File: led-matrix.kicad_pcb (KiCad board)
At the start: 2 copper layers, 91 parts, among them J1 Conn_01x01_Pin, J10 Conn_01x01_Pin, J11 Conn_01x01_Pin, J12 Conn_01x01_Pin, J13 Conn_01x01_Pin, J14 Conn_01x01_Pin, J15 Conn_01x01_Pin, J16 Conn_01x01_Pin, J17 Conn_01x01_Pin, J18 Conn_01x01_Pin, J19 Conn_01x01_Pin, J2 Conn_01x01_Pin, J20 Conn_01x01_Pin, J21 Conn_01x01_Pin, J22 Conn_01x01_Pin, J23 Conn_01x01_Pin, J3 Conn_01x01_Pin, J4 Conn_01x01_Pin, J5 Conn_01x01_Pin, J6 Conn_01x01_Pin, J7 Conn_01x01_Pin, J8 Conn_01x01_Pin, J9 Conn_01x01_Pin, U1 MAX7219, U2 Pico

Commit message: feat: layout basic pcb design
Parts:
- moved J6 77.9 mm to (126.0, 65.0)
- moved J1 77.8 mm to (96.0, 65.0)
- moved J5 76.4 mm to (120.0, 65.0)
- moved J2 76.4 mm to (102.0, 65.0)
- moved J4 75.7 mm to (114.0, 65.0)
- moved J3 75.7 mm to (108.0, 65.0)
- moved J12 72.5 mm to (159.5, 64.5)
- moved J11 68.3 mm to (154.0, 64.5)
- moved J10 64.7 mm to (148.5, 64.5)
- moved J9 61.8 mm to (143.0, 64.5)
- moved J8 59.4 mm to (137.5, 64.5)
- moved J7 57.9 mm to (132.0, 64.5)
- moved J14 54.8 mm to (170.5, 64.5)
- moved J15 53.1 mm to (173.0, 71.0)
- moved J16 52.0 mm to (173.0, 76.5)
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
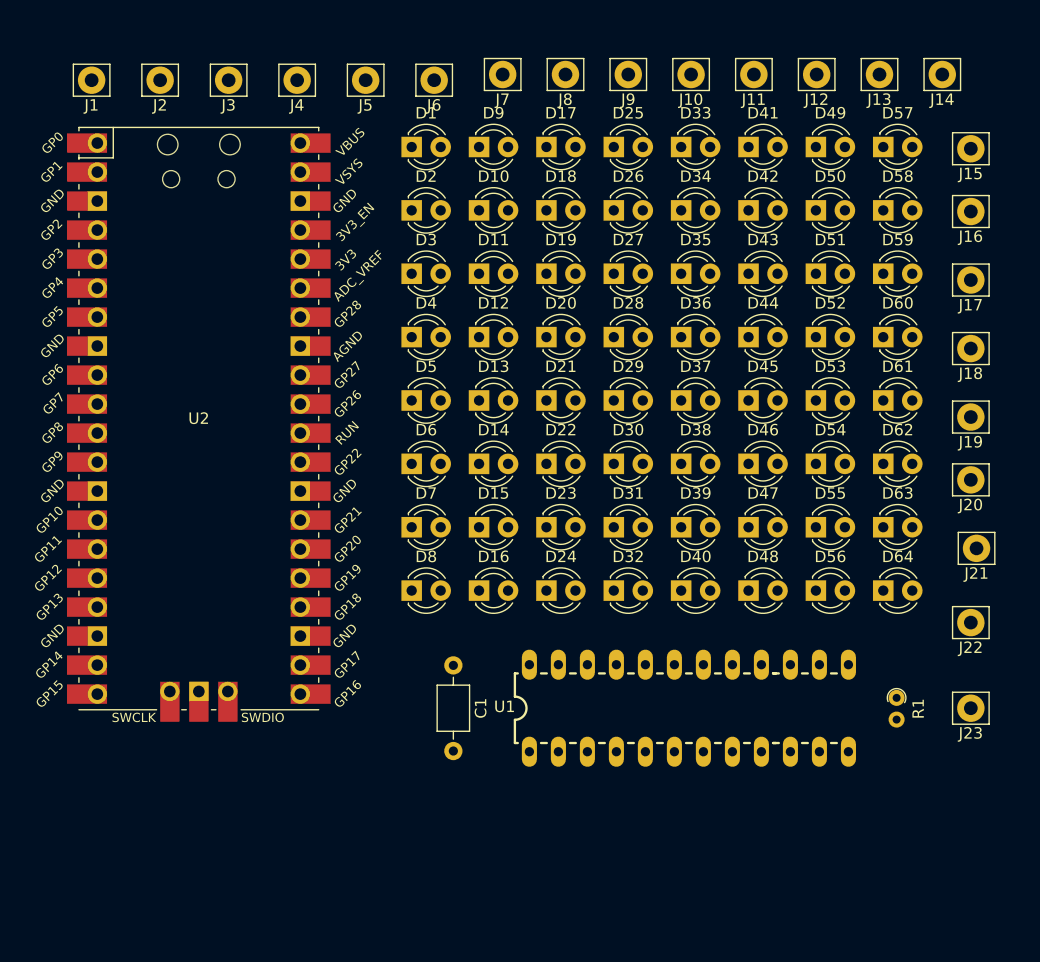
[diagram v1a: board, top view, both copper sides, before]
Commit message: chore: align and center the gpio
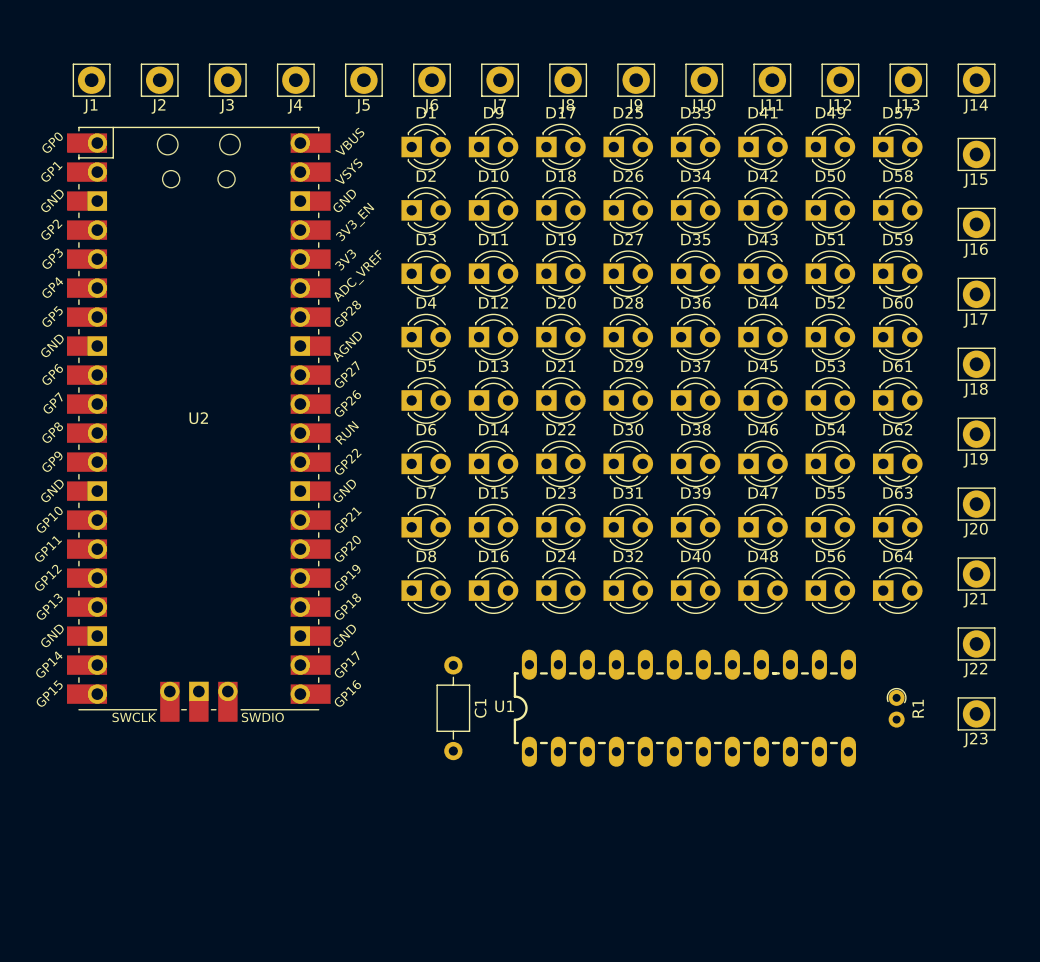
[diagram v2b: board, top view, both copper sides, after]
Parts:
- moved J14 3.04 mm to (173.5, 65.0)
- moved J13 2.59 mm to (167.5, 65.0)
- moved J21 2.25 mm to (173.5, 108.2)
- moved J20 2.18 mm to (173.5, 102.1)
- moved J12 2.14 mm to (161.6, 65.0)
- moved J22 1.94 mm to (173.5, 114.4)
- moved J11 1.69 mm to (155.6, 65.0)
- moved J19 1.58 mm to (173.5, 96.0)
- moved J18 1.46 mm to (173.5, 89.9)
- moved J17 1.35 mm to (173.5, 83.8)
- moved J10 1.26 mm to (149.7, 65.0)
- moved J16 1.23 mm to (173.5, 77.6)
- moved J9 0.85 mm to (143.7, 65.0)
- moved J15 0.71 mm to (173.5, 71.5)
- moved J23 0.71 mm to (173.5, 120.5)
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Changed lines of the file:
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@@
 	(footprint "Connector_Pin:Pin_D1.2mm_L11.3mm_W3.0mm_Flat"
 		(layer "F.Cu")
-		(at 173 100)
+		(at 173.5 102.125)
 		(descr "solder Pin_ with flat with hole, hole diameter 1.2mm, length 11.3mm, width 3.0mm")
 		(tags "solder Pin_ with flat fork")
@@
 	(footprint "Connector_Pin:Pin_D1.2mm_L11.3mm_W3.0mm_Flat"
 		(layer "F.Cu")
-		(at 137.5 64.5)
+		(at 137.730766 65)
 		(descr "solder Pin_ with flat with hole, hole diameter 1.2mm, length 11.3mm, width 3.0mm")
 		(tags "solder Pin_ with flat fork")
@@
 	(footprint "Connector_Pin:Pin_D1.2mm_L11.3mm_W3.0mm_Flat"
 		(layer "F.Cu")
-		(at 173.5 106)
+		(at 173.5 108.25)
 		(descr "solder Pin_ with flat with hole, hole diameter 1.2mm, length 11.3mm, width 3.0mm")
 		(tags "solder Pin_ with flat fork")
@@
 	(footprint "Connector_Pin:Pin_D1.2mm_L11.3mm_W3.0mm_Flat"
 		(layer "F.Cu")
-		(at 170.5 64.5)
+		(at 173.5 65)
 		(descr "solder Pin_ with flat with hole, hole diameter 1.2mm, length 11.3mm, width 3.0mm")
 		(tags "solder Pin_ with flat fork")
@@
 	(footprint "Connector_Pin:Pin_D1.2mm_L11.3mm_W3.0mm_Flat"
 		(layer "F.Cu")
-		(at 173 88.5)
+		(at 173.5 89.875)
 		(descr "solder Pin_ with flat with hole, hole diameter 1.2mm, length 11.3mm, width 3.0mm")
 		(tags "solder Pin_ with flat fork")
@@
 	(footprint "Connector_Pin:Pin_D1.2mm_L11.3mm_W3.0mm_Flat"
 		(layer "F.Cu")
-		(at 165 64.5)
+		(at 167.538456 65)
 		(descr "solder Pin_ with flat with hole, hole diameter 1.2mm, length 11.3mm, width 3.0mm")
 		(tags "solder Pin_ with flat fork")
@@
 		)
 		(property "Value" "Conn_01x01_Pin"
-			(at 0 -2.05 0)
+			(at 3 -2.05 0)
 			(layer "F.Fab")
 			(effects
@@
 	(footprint "Connector_Pin:Pin_D1.2mm_L11.3mm_W3.0mm_Flat"
 		(layer "F.Cu")
-		(at 102 65)
+		(at 101.961538 65)
 		(descr "solder Pin_ with flat with hole, hole diameter 1.2mm, length 11.3mm, width 3.0mm")
 		(tags "solder Pin_ with flat fork")
@@
 	(footprint "Connector_Pin:Pin_D1.2mm_L11.3mm_W3.0mm_Flat"
 		(layer "F.Cu")
-		(at 173 76.5)
+		(at 173.5 77.625)
 		(descr "solder Pin_ with flat with hole, hole diameter 1.2mm, length 11.3mm, width 3.0mm")
 		(tags "solder Pin_ with flat fork")
@@
 	(footprint "Connector_Pin:Pin_D1.2mm_L11.3mm_W3.0mm_Flat"
 		(layer "F.Cu")
-		(at 108 65)
+		(at 107.923076 65)
 		(descr "solder Pin_ with flat with hole, hole diameter 1.2mm, length 11.3mm, width 3.0mm")
 		(tags "solder Pin_ with flat fork")
@@
 	(footprint "Connector_Pin:Pin_D1.2mm_L11.3mm_W3.0mm_Flat"
 		(layer "F.Cu")
-		(at 173 71)
+		(at 173.5 71.5)
 		(descr "solder Pin_ with flat with hole, hole diameter 1.2mm, length 11.3mm, width 3.0mm")
 		(tags "solder Pin_ with flat fork")
@@
 	(footprint "Connector_Pin:Pin_D1.2mm_L11.3mm_W3.0mm_Flat"
 		(layer "F.Cu")
-		(at 173 94.5)
+		(at 173.5 96)
 		(descr "solder Pin_ with flat with hole, hole diameter 1.2mm, length 11.3mm, width 3.0mm")
 		(tags "solder Pin_ with flat fork")
@@
 	(footprint "Connector_Pin:Pin_D1.2mm_L11.3mm_W3.0mm_Flat"
 		(layer "F.Cu")
-		(at 159.5 64.5)
+		(at 161.576918 65)
 		(descr "solder Pin_ with flat with hole, hole diameter 1.2mm, length 11.3mm, width 3.0mm")
 		(tags "solder Pin_ with flat fork")
@@
 	(footprint "Connector_Pin:Pin_D1.2mm_L11.3mm_W3.0mm_Flat"
 		(layer "F.Cu")
-		(at 173 112.5)
+		(at 173.5 114.375)
 		(descr "solder Pin_ with flat with hole, hole diameter 1.2mm, length 11.3mm, width 3.0mm")
 		(tags "solder Pin_ with flat fork")
@@
 	(footprint "Connector_Pin:Pin_D1.2mm_L11.3mm_W3.0mm_Flat"
 		(layer "F.Cu")
-		(at 173 120)
+		(at 173.5 120.5)
 		(descr "solder Pin_ with flat with hole, hole diameter 1.2mm, length 11.3mm, width 3.0mm")
 		(tags "solder Pin_ with flat fork")
@@
 	(footprint "Connector_Pin:Pin_D1.2mm_L11.3mm_W3.0mm_Flat"
 		(layer "F.Cu")
-		(at 120 65)
+		(at 119.846152 65)
 		(descr "solder Pin_ with flat with hole, hole diameter 1.2mm, length 11.3mm, width 3.0mm")
 		(tags "solder Pin_ with flat fork")
@@
 	(footprint "Connector_Pin:Pin_D1.2mm_L11.3mm_W3.0mm_Flat"
 		(layer "F.Cu")
-		(at 114 65)
+		(at 113.884614 65)
 		(descr "solder Pin_ with flat with hole, hole diameter 1.2mm, length 11.3mm, width 3.0mm")
 		(tags "solder Pin_ with flat fork")
@@
 	(footprint "Connector_Pin:Pin_D1.2mm_L11.3mm_W3.0mm_Flat"
 		(layer "F.Cu")
-		(at 148.5 64.5)
+		(at 149.653842 65)
 		(descr "solder Pin_ with flat with hole, hole diameter 1.2mm, length 11.3mm, width 3.0mm")
 		(tags "solder Pin_ with flat fork")
@@
 	(footprint "Connector_Pin:Pin_D1.2mm_L11.3mm_W3.0mm_Flat"
 		(layer "F.Cu")
-		(at 132 64.5)
+		(at 131.769228 65)
 		(descr "solder Pin_ with flat with hole, hole diameter 1.2mm, length 11.3mm, width 3.0mm")
 		(tags "solder Pin_ with flat fork")
@@
 	(footprint "Connector_Pin:Pin_D1.2mm_L11.3mm_W3.0mm_Flat"
 		(layer "F.Cu")
-		(at 173 82.5)
+		(at 173.5 83.75)
 		(descr "solder Pin_ with flat with hole, hole diameter 1.2mm, length 11.3mm, width 3.0mm")
 		(tags "solder Pin_ with flat fork")
@@
 	(footprint "Connector_Pin:Pin_D1.2mm_L11.3mm_W3.0mm_Flat"
 		(layer "F.Cu")
-		(at 143 64.5)
+		(at 143.692304 65)
 		(descr "solder Pin_ with flat with hole, hole diameter 1.2mm, length 11.3mm, width 3.0mm")
 		(tags "solder Pin_ with flat fork")
@@
 	(footprint "Connector_Pin:Pin_D1.2mm_L11.3mm_W3.0mm_Flat"
 		(layer "F.Cu")
-		(at 126 65)
+		(at 125.80769 65)
 		(descr "solder Pin_ with flat with hole, hole diameter 1.2mm, length 11.3mm, width 3.0mm")
 		(tags "solder Pin_ with flat fork")
@@
 	(footprint "Connector_Pin:Pin_D1.2mm_L11.3mm_W3.0mm_Flat"
 		(layer "F.Cu")
-		(at 154 64.5)
+		(at 155.61538 65)
 		(descr "solder Pin_ with flat with hole, hole diameter 1.2mm, length 11.3mm, width 3.0mm")
 		(tags "solder Pin_ with flat fork")

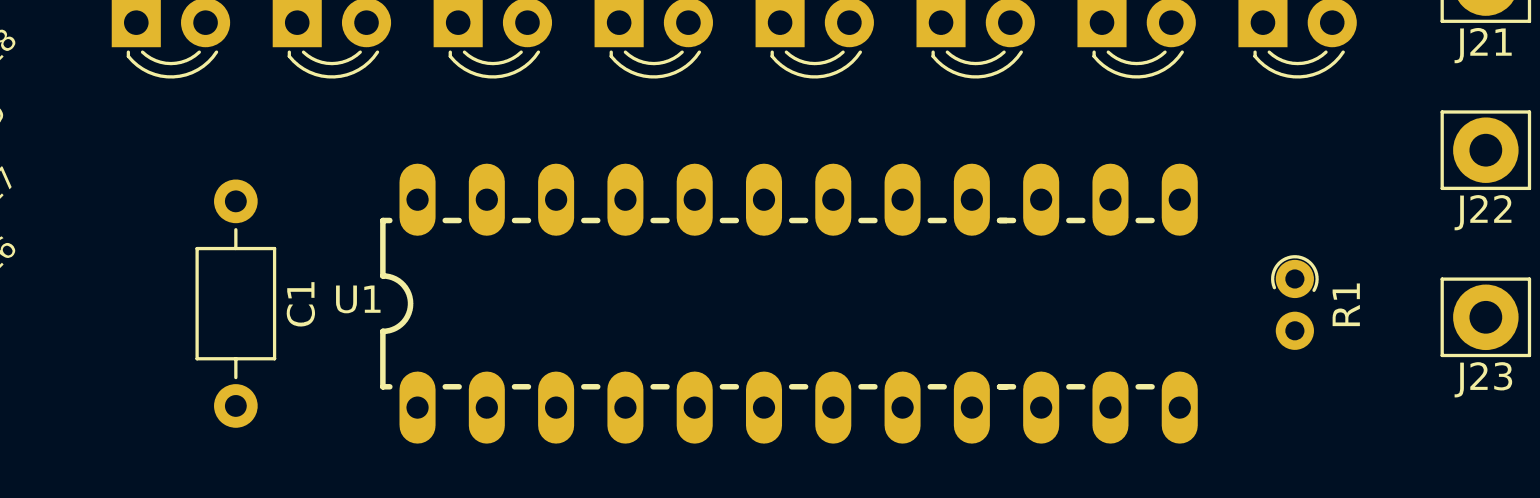
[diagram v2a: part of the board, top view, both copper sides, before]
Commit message: chore: make resister bigger and align max7219 and cap / resister
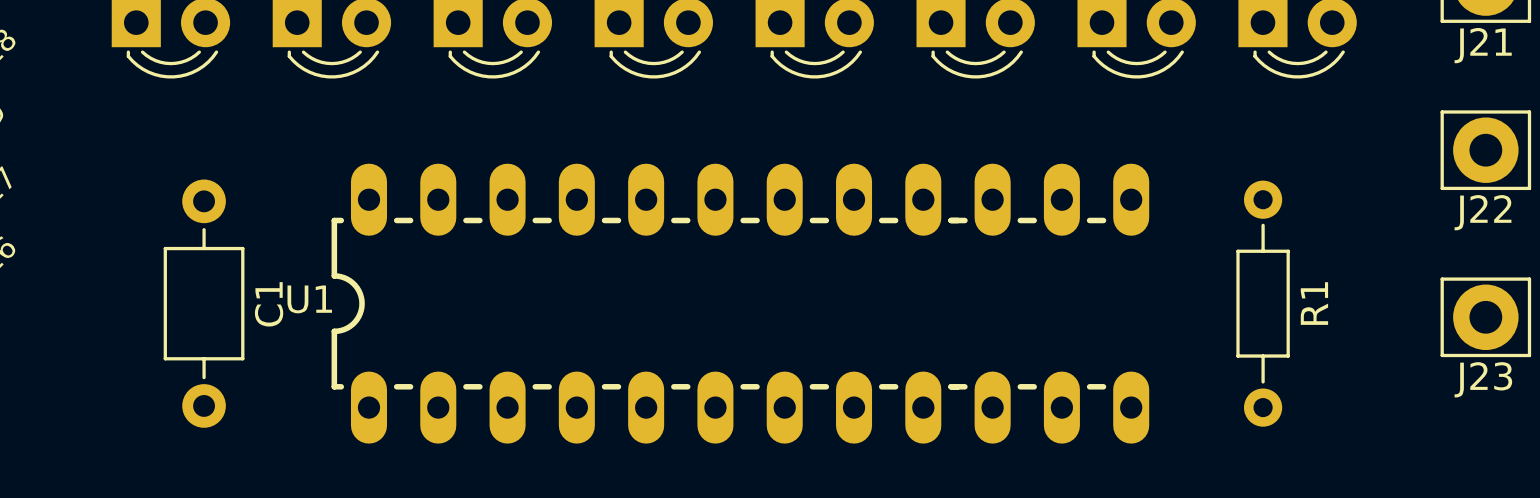
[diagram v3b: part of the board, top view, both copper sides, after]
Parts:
- R1: footprint Resistor_THT:R_Axial_DIN0204_L3.6mm_D1.6mm_P1.90mm_Vertical -> Resistor_THT:R_Axial_DIN0204_L3.6mm_D1.6mm_P7.62mm_Horizontal
- moved R1 3.13 mm to (165.3, 116.2)
- moved U1 1.78 mm to (146.5, 120.0)
- moved C1 1.17 mm to (126.5, 116.2)
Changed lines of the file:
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@@
 		)
 	)
-	(footprint "Resistor_THT:R_Axial_DIN0204_L3.6mm_D1.6mm_P1.90mm_Vertical"
+	(footprint "Resistor_THT:R_Axial_DIN0204_L3.6mm_D1.6mm_P7.62mm_Horizontal"
 		(layer "F.Cu")
-		(at 166.5 119.095 -90)
-		(descr "Resistor, Axial_DIN0204 series, Axial, Vertical, pin pitch=1.9mm, 0.167W, length*diameter=3.6*1.6mm^2, http://cdn-reichelt.de/documents/datenblatt/B400/1_4W%23YAG.pdf")
-		(tags "Resistor Axial_DIN0204 series Axial Vertical pin pitch 1.9mm 0.167W length 3.6mm diameter 1.6mm")
+		(at 165.3344 116.19 -90)
+		(descr "Resistor, Axial_DIN0204 series, Axial, Horizontal, pin pitch=7.62mm, 0.167W, length*diameter=3.6*1.6mm^2, http://cdn-reichelt.de/documents/datenblatt/B400/1_4W%23YAG.pdf")
+		(tags "Resistor Axial_DIN0204 series Axial Horizontal pin pitch 7.62mm 0.167W length 3.6mm diameter 1.6mm")
 		(property "Reference" "R1"
-			(at 0.95 -1.92 90)
+			(at 3.81 -1.92 -90)
 			(layer "F.SilkS")
 			(effects
@@
 		)
 		(property "Value" "100k"
-			(at 0.95 1.92 90)
+			(at 3.81 1.92 -90)
 			(layer "F.Fab")
 			(effects
@@
 			)
 		)
-		(property "Footprint" "Resistor_THT:R_Axial_DIN0204_L3.6mm_D1.6mm_P1.90mm_Vertical"
+		(property "Footprint" "Resistor_THT:R_Axial_DIN0204_L3.6mm_D1.6mm_P7.62mm_Horizontal"
 			(at 0 0 -90)
 			(unlocked yes)
@@
 		(sheetfile "led-matrix.kicad_sch")
 		(attr through_hole)
-		(fp_arc
-			(start 0.320095 0.749359)
-			(mid -0.813042 -0.054435)
-			(end 0.417133 -0.7)
+		(fp_line
+			(start 1.89 0.92)
+			(end 5.73 0.92)
+			(stroke
+				(width 0.12)
+				(type solid)
+			)
+			(layer "F.SilkS")
+		)
+		(fp_line
+			(start 5.73 0.92)
+			(end 5.73 -0.92)
+			(stroke
+				(width 0.12)
+				(type solid)
+			)
+			(layer "F.SilkS")
+		)
+		(fp_line
+			(start 0.94 0)
+			(end 1.89 0)
+			(stroke
+				(width 0.12)
+				(type solid)
+			)
+			(layer "F.SilkS")
+		)
+		(fp_line
+			(start 6.68 0)
+			(end 5.73 0)
+			(stroke
+				(width 0.12)
+				(type solid)
+			)
+			(layer "F.SilkS")
+		)
+		(fp_line
+			(start 1.89 -0.92)
+			(end 1.89 0.92)
+			(stroke
+				(width 0.12)
+				(type solid)
+			)
+			(layer "F.SilkS")
+		)
+		(fp_line
+			(start 5.73 -0.92)
+			(end 1.89 -0.92)
 			(stroke
 				(width 0.12)
@@
 		)
 		(fp_line
-			(start -1.05 1.05)
-			(end 2.86 1.05)
+			(start -0.95 1.05)
+			(end 8.57 1.05)
 			(stroke
 				(width 0.05)
@@
 		)
 		(fp_line
-			(start 2.86 1.05)
-			(end 2.86 -1.05)
+			(start 8.57 1.05)
+			(end 8.57 -1.05)
 			(stroke
 				(width 0.05)
@@
 		)
 		(fp_line
-			(start -1.05 -1.05)
-			(end -1.05 1.05)
+			(start -0.95 -1.05)
+			(end -0.95 1.05)
 			(stroke
 				(width 0.05)
@@
 		)
 		(fp_line
-			(start 2.86 -1.05)
-			(end -1.05 -1.05)
+			(start 8.57 -1.05)
+			(end -0.95 -1.05)
 			(stroke
 				(width 0.05)
@@
 		)
 		(fp_line
+			(start 2.01 0.8)
+			(end 5.61 0.8)
+			(stroke
+				(width 0.1)
+				(type solid)
+			)
+			(layer "F.Fab")
+		)
+		(fp_line
+			(start 5.61 0.8)
+			(end 5.61 -0.8)
+			(stroke
+				(width 0.1)
+				(type solid)
+			)
+			(layer "F.Fab")
+		)
+		(fp_line
 			(start 0 0)
-			(end 1.9 0)
+			(end 2.01 0)
 			(stroke
 				(width 0.1)
@@
 			(layer "F.Fab")
 		)
-		(fp_circle
-			(center 0 0)
-			(end 0.8 0)
+		(fp_line
+			(start 7.62 0)
+			(end 5.61 0)
+			(stroke
+				(width 0.1)
+				(type solid)
+			)
+			(layer "F.Fab")
+		)
+		(fp_line
+			(start 2.01 -0.8)
+			(end 2.01 0.8)
+			(stroke
+				(width 0.1)
+				(type solid)
+			)
+			(layer "F.Fab")
+		)
+		(fp_line
+			(start 5.61 -0.8)
+			(end 2.01 -0.8)
 			(stroke
 				(width 0.1)
 				(type solid)
 			)
-			(fill none)
 			(layer "F.Fab")
 		)
 		(fp_text user "${REFERENCE}"
-			(at 0.95 -1.92 90)
+			(at 3.81 0 -90)
 			(layer "F.Fab")
 			(effects
 				(font
-					(size 1 1)
-					(thickness 0.15)
+					(size 0.72 0.72)
+					(thickness 0.108)
 				)
 			)
@@
 		)
 		(pad "2" thru_hole oval
-			(at 1.9 0 270)
+			(at 7.62 0 270)
 			(size 1.4 1.4)
 			(drill 0.7)
@@
 			(pintype "passive")
 		)
-		(model "${KICAD8_3DMODEL_DIR}/Resistor_THT.3dshapes/R_Axial_DIN0204_L3.6mm_D1.6mm_P1.90mm_Vertical.wrl"
+		(model "${KICAD8_3DMODEL_DIR}/Resistor_THT.3dshapes/R_Axial_DIN0204_L3.6mm_D1.6mm_P7.62mm_Horizontal.wrl"
 			(offset
 				(xyz 0 0 0)
@@
 	(footprint "Capacitor_THT:C_Axial_L3.8mm_D2.6mm_P7.50mm_Horizontal"
 		(layer "F.Cu")
-		(at 127.68 116.25 -90)
+		(at 126.5144 116.25 -90)
 		(descr "C, Axial series, Axial, Horizontal, pin pitch=7.5mm, , length*diameter=3.8*2.6mm^2, http://www.vishay.com/docs/45231/arseries.pdf")
 		(tags "C Axial series Axial Horizontal pin pitch 7.5mm  length 3.8mm diameter 2.6mm")
@@
 	(footprint "max7219:DIL24"
 		(layer "F.Cu")
-		(at 148.31 120)
+		(at 146.53 120)
 		(property "Reference" "U1"
 			(at -16.137745 -0.127075 180)
